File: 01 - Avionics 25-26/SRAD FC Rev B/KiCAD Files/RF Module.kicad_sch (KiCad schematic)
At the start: 1 part, among them U2 RA-01H

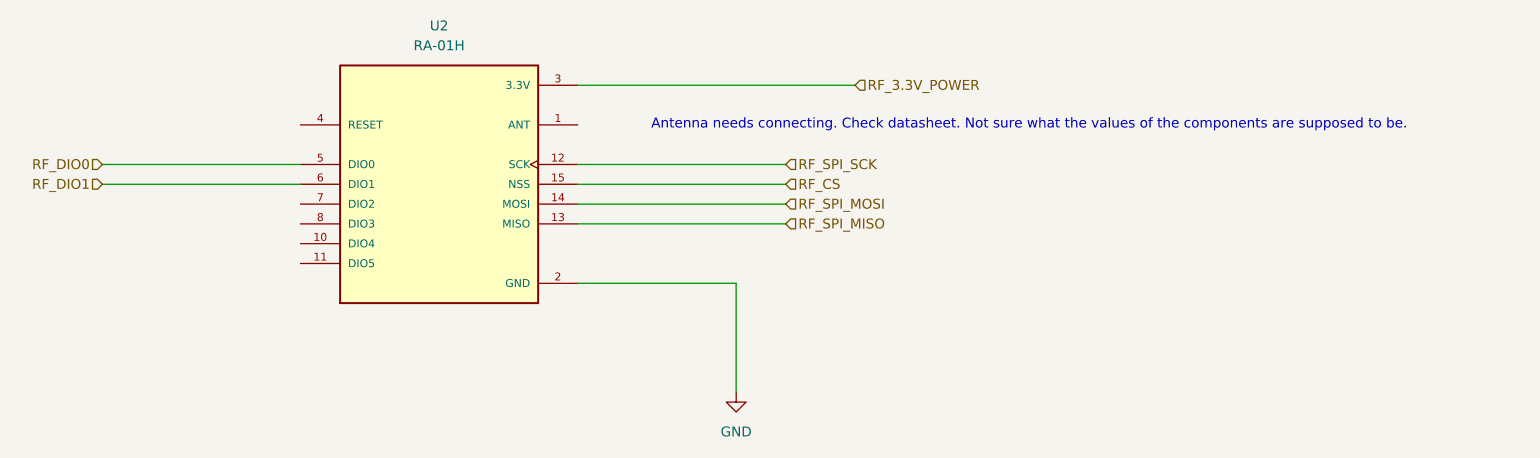
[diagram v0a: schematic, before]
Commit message: added antenna for new rf module
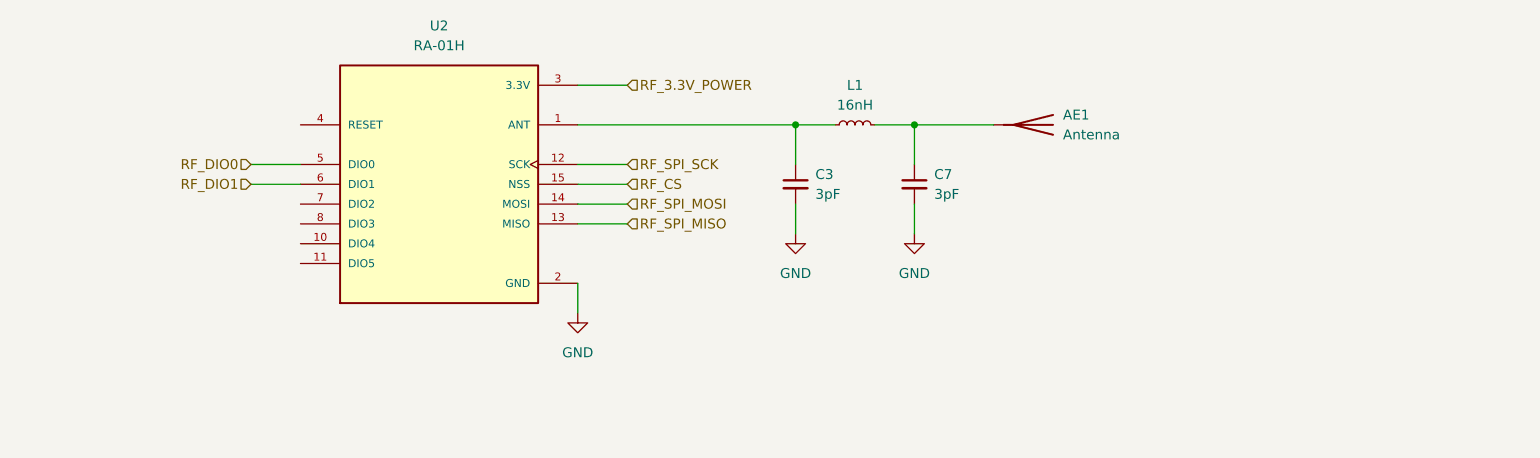
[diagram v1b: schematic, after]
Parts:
- added AE1: Antenna, symbol Device:Antenna
- added C3, C7: 3pF, symbol Device:C_Small
- added L1: 16nH, symbol Device:L_Small
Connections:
- net GND: now also C3.2, C7.2
- net at U2.1 (ANT): now also C3.1, L1.1
- new net: AE1.1 (A), C7.1, L1.2
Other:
- note removed: "Antenna needs connecting. Check datasheet. Not sure what the values of the components are supposed to be."
